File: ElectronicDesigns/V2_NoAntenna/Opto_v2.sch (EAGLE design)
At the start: 7 parts, among them U1 TLV1117-18IDCYG3

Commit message: Presentation
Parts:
- removed C2: 06036D225KAT2A, Capacitor_2.2uF_0603:06036D225KAT2A
- removed U$2: B220A-13-F, Schottky_0603:B220A-13-F
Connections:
- removed net IN-: C1.2, U$2.C
- net GND: now also C1.2; no longer C2.2, U$2.A
- net N$4: no longer C2.1
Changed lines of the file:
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@@
 <parts>
 <part name="GND1" library="supply1" library_urn="urn:adsk.eagle:library:371" deviceset="GND" device=""/>
-<part name="GND2" library="supply1" library_urn="urn:adsk.eagle:library:371" deviceset="GND" device=""/>
 <part name="R1" library="CRCW06033K30FKEA" deviceset="CRCW06033K30FKEA" device=""/>
 <part name="U1" library="TLV1117-18IDCYG3" deviceset="TLV1117-18IDCYG3" device=""/>
 <part name="U$1" library="Schottky_0603" deviceset="B220A-13-F" device=""/>
-<part name="U$2" library="Schottky_0603" deviceset="B220A-13-F" device=""/>
 <part name="C1" library="Capacitor_2.2uF_0603" deviceset="06036D225KAT2A" device=""/>
-<part name="C2" library="Capacitor_2.2uF_0603" deviceset="06036D225KAT2A" device=""/>
 <part name="U$3" library="LEDM1608X80" deviceset="LED" device=""/>
 </parts>
@@
 </plain>
 <instances>
-<instance part="GND1" gate="1" x="40.64" y="35.56"/>
-<instance part="GND2" gate="1" x="88.9" y="35.56"/>
+<instance part="GND1" gate="1" x="48.26" y="35.56"/>
 <instance part="R1" gate="G$1" x="114.3" y="63.5"/>
 <instance part="U1" gate="A" x="68.58" y="66.04"/>
 <instance part="U$1" gate="A" x="10.16" y="71.12"/>
-<instance part="U$2" gate="A" x="12.7" y="43.18" rot="R180"/>
 <instance part="C1" gate="G$1" x="-10.16" y="55.88" rot="R90"/>
-<instance part="C2" gate="G$1" x="30.48" y="55.88" rot="R90"/>
 <instance part="U$3" gate="G$1" x="137.16" y="63.5"/>
 </instances>
@@
 </segment>
 </net>
-<net name="IN-" class="0">
-<segment>
-<wire x1="10.16" y1="43.18" x2="-10.16" y2="43.18" width="0.1524" layer="91"/>
-<label x="-35.56" y="43.18" size="1.778" layer="95" rot="R180" xref="yes"/>
-<pinref part="U$2" gate="A" pin="C"/>
-<pinref part="C1" gate="G$1" pin="2"/>
-<wire x1="-10.16" y1="43.18" x2="-35.56" y2="43.18" width="0.1524" layer="91"/>
-<wire x1="-10.16" y1="53.34" x2="-10.16" y2="43.18" width="0.1524" layer="91"/>
-<junction x="-10.16" y="43.18"/>
-</segment>
-</net>
 <net name="N$4" class="0">
 <segment>
-<wire x1="48.26" y1="71.12" x2="30.48" y2="71.12" width="0.1524" layer="91"/>
 <pinref part="U1" gate="A" pin="INPUT"/>
-<wire x1="30.48" y1="71.12" x2="12.7" y2="71.12" width="0.1524" layer="91"/>
+<wire x1="48.26" y1="71.12" x2="12.7" y2="71.12" width="0.1524" layer="91"/>
 <wire x1="48.26" y1="66.04" x2="48.26" y2="71.12" width="0.1524" layer="91"/>
 <pinref part="U$1" gate="A" pin="C"/>
-<pinref part="C2" gate="G$1" pin="1"/>
-<wire x1="30.48" y1="60.96" x2="30.48" y2="71.12" width="0.1524" layer="91"/>
-<junction x="30.48" y="71.12"/>
-</segment>
-</net>
-<net name="GND" class="0">
-<segment>
-<wire x1="15.24" y1="43.18" x2="30.48" y2="43.18" width="0.1524" layer="91"/>
-<junction x="40.64" y="43.18"/>
-<pinref part="GND1" gate="1" pin="GND"/>
-<wire x1="30.48" y1="43.18" x2="40.64" y2="43.18" width="0.1524" layer="91"/>
-<wire x1="40.64" y1="38.1" x2="40.64" y2="43.18" width="0.1524" layer="91"/>
-<pinref part="U1" gate="A" pin="ADJ/GND"/>
-<wire x1="48.26" y1="58.42" x2="48.26" y2="43.18" width="0.1524" layer="91"/>
-<wire x1="48.26" y1="43.18" x2="40.64" y2="43.18" width="0.1524" layer="91"/>
-<pinref part="U$2" gate="A" pin="A"/>
-<pinref part="C2" gate="G$1" pin="2"/>
-<wire x1="30.48" y1="53.34" x2="30.48" y2="43.18" width="0.1524" layer="91"/>
-<junction x="30.48" y="43.18"/>
-</segment>
-<segment>
-<pinref part="GND2" gate="1" pin="GND"/>
-<wire x1="88.9" y1="38.1" x2="88.9" y2="53.34" width="0.1524" layer="91"/>
-<wire x1="154.94" y1="63.5" x2="154.94" y2="53.34" width="0.1524" layer="91"/>
-<wire x1="154.94" y1="53.34" x2="88.9" y2="53.34" width="0.1524" layer="91"/>
-<pinref part="U$3" gate="G$1" pin="OUT"/>
-<wire x1="147.32" y1="63.5" x2="154.94" y2="63.5" width="0.1524" layer="91"/>
 </segment>
 </net>
@@
 </segment>
 </net>
+<net name="GND" class="0">
+<segment>
+<pinref part="U1" gate="A" pin="ADJ/GND"/>
+<wire x1="48.26" y1="58.42" x2="48.26" y2="43.18" width="0.1524" layer="91"/>
+<wire x1="48.26" y1="43.18" x2="-10.16" y2="43.18" width="0.1524" layer="91"/>
+<label x="-35.56" y="43.18" size="1.778" layer="95" rot="R180" xref="yes"/>
+<pinref part="C1" gate="G$1" pin="2"/>
+<wire x1="-10.16" y1="43.18" x2="-35.56" y2="43.18" width="0.1524" layer="91"/>
+<wire x1="-10.16" y1="53.34" x2="-10.16" y2="43.18" width="0.1524" layer="91"/>
+<junction x="-10.16" y="43.18"/>
+<pinref part="U$3" gate="G$1" pin="OUT"/>
+<wire x1="147.32" y1="63.5" x2="154.94" y2="63.5" width="0.1524" layer="91"/>
+<wire x1="154.94" y1="63.5" x2="154.94" y2="43.18" width="0.1524" layer="91"/>
+<wire x1="154.94" y1="43.18" x2="48.26" y2="43.18" width="0.1524" layer="91"/>
+<junction x="48.26" y="43.18"/>
+<pinref part="GND1" gate="1" pin="GND"/>
+<wire x1="48.26" y1="38.1" x2="48.26" y2="43.18" width="0.1524" layer="91"/>
+</segment>
+</net>

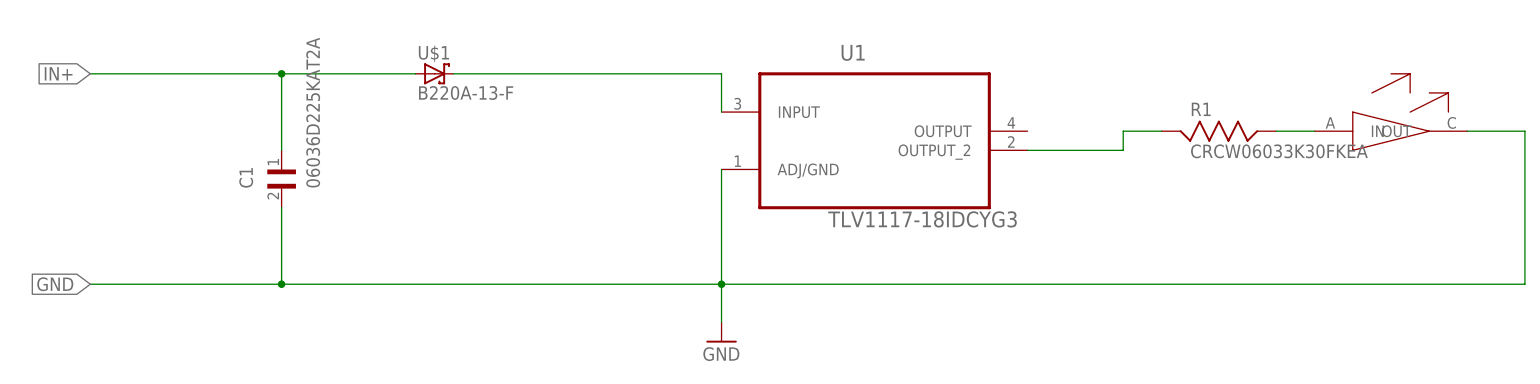
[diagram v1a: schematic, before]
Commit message: antenna-circuit assembled
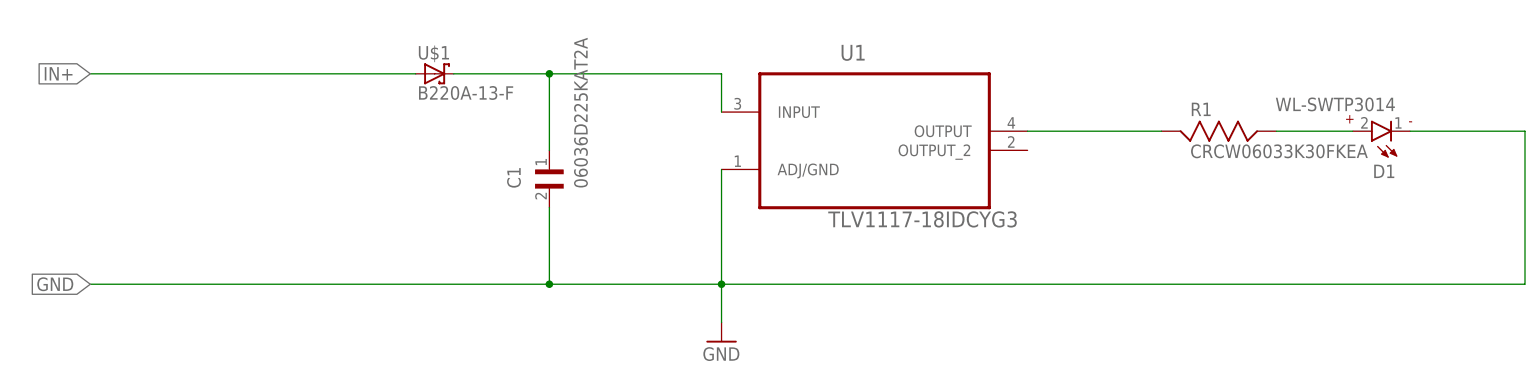
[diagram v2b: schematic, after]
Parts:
- removed U$3: LED, LEDM1608X80:LED
- added D1: WL-SWTP3014, WL-SWTP:WL-SWTP3014
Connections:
- net GND: now also D1.1; no longer U$3.OUT
- net IN+: no longer C1.1
- net N$1: now also U1.OUTPUT; no longer U1.OUTPUT_2
- net N$2: now also D1.2; no longer U$3.IN
- net N$4: now also C1.1
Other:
- moved on the sheet: C1
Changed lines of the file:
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@@
 <part name="U$1" library="Schottky_0603" deviceset="B220A-13-F" device=""/>
 <part name="C1" library="Capacitor_2.2uF_0603" deviceset="06036D225KAT2A" device=""/>
-<part name="U$3" library="LEDM1608X80" deviceset="LED" device=""/>
+<part name="D1" library="WL-SWTP" deviceset="WL-SWTP" device="3014"/>
 </parts>
 <sheets>
@@
 <instance part="U1" gate="A" x="68.58" y="66.04"/>
 <instance part="U$1" gate="A" x="10.16" y="71.12"/>
-<instance part="C1" gate="G$1" x="-10.16" y="55.88" rot="R90"/>
-<instance part="U$3" gate="G$1" x="137.16" y="63.5"/>
+<instance part="C1" gate="G$1" x="25.4" y="55.88" rot="R90"/>
+<instance part="D1" gate="G$1" x="137.16" y="63.5" rot="R180"/>
 </instances>
 <busses>
@@
 <net name="IN+" class="0">
 <segment>
-<wire x1="7.62" y1="71.12" x2="-10.16" y2="71.12" width="0.1524" layer="91"/>
 <label x="-35.56" y="71.12" size="1.778" layer="95" rot="R180" xref="yes"/>
 <pinref part="U$1" gate="A" pin="A"/>
-<pinref part="C1" gate="G$1" pin="1"/>
-<wire x1="-10.16" y1="71.12" x2="-35.56" y2="71.12" width="0.1524" layer="91"/>
-<wire x1="-10.16" y1="60.96" x2="-10.16" y2="71.12" width="0.1524" layer="91"/>
-<junction x="-10.16" y="71.12"/>
+<wire x1="7.62" y1="71.12" x2="-35.56" y2="71.12" width="0.1524" layer="91"/>
 </segment>
 </net>
@@
 <segment>
 <pinref part="U1" gate="A" pin="INPUT"/>
-<wire x1="48.26" y1="71.12" x2="12.7" y2="71.12" width="0.1524" layer="91"/>
+<wire x1="48.26" y1="71.12" x2="25.4" y2="71.12" width="0.1524" layer="91"/>
+<wire x1="25.4" y1="71.12" x2="12.7" y2="71.12" width="0.1524" layer="91"/>
 <wire x1="48.26" y1="66.04" x2="48.26" y2="71.12" width="0.1524" layer="91"/>
 <pinref part="U$1" gate="A" pin="C"/>
+<pinref part="C1" gate="G$1" pin="1"/>
+<wire x1="25.4" y1="60.96" x2="25.4" y2="71.12" width="0.1524" layer="91"/>
+<junction x="25.4" y="71.12"/>
 </segment>
 </net>
 <net name="N$1" class="0">
 <segment>
-<pinref part="U1" gate="A" pin="OUTPUT_2"/>
-<wire x1="88.9" y1="60.96" x2="101.6" y2="60.96" width="0.1524" layer="91"/>
-<wire x1="101.6" y1="60.96" x2="101.6" y2="63.5" width="0.1524" layer="91"/>
 <pinref part="R1" gate="G$1" pin="1"/>
-<wire x1="101.6" y1="63.5" x2="106.68" y2="63.5" width="0.1524" layer="91"/>
-</segment>
-</net>
-<net name="N$2" class="0">
-<segment>
-<pinref part="U$3" gate="G$1" pin="IN"/>
-<pinref part="R1" gate="G$1" pin="2"/>
-<wire x1="127" y1="63.5" x2="121.92" y2="63.5" width="0.1524" layer="91"/>
+<pinref part="U1" gate="A" pin="OUTPUT"/>
+<wire x1="88.9" y1="63.5" x2="106.68" y2="63.5" width="0.1524" layer="91"/>
 </segment>
 </net>
@@
 <pinref part="U1" gate="A" pin="ADJ/GND"/>
 <wire x1="48.26" y1="58.42" x2="48.26" y2="43.18" width="0.1524" layer="91"/>
-<wire x1="48.26" y1="43.18" x2="-10.16" y2="43.18" width="0.1524" layer="91"/>
+<wire x1="48.26" y1="43.18" x2="25.4" y2="43.18" width="0.1524" layer="91"/>
 <label x="-35.56" y="43.18" size="1.778" layer="95" rot="R180" xref="yes"/>
-<pinref part="C1" gate="G$1" pin="2"/>
-<wire x1="-10.16" y1="43.18" x2="-35.56" y2="43.18" width="0.1524" layer="91"/>
-<wire x1="-10.16" y1="53.34" x2="-10.16" y2="43.18" width="0.1524" layer="91"/>
-<junction x="-10.16" y="43.18"/>
-<pinref part="U$3" gate="G$1" pin="OUT"/>
-<wire x1="147.32" y1="63.5" x2="154.94" y2="63.5" width="0.1524" layer="91"/>
+<wire x1="25.4" y1="43.18" x2="-35.56" y2="43.18" width="0.1524" layer="91"/>
 <wire x1="154.94" y1="63.5" x2="154.94" y2="43.18" width="0.1524" layer="91"/>
 <wire x1="154.94" y1="43.18" x2="48.26" y2="43.18" width="0.1524" layer="91"/>
@@
 <pinref part="GND1" gate="1" pin="GND"/>
 <wire x1="48.26" y1="38.1" x2="48.26" y2="43.18" width="0.1524" layer="91"/>
+<pinref part="C1" gate="G$1" pin="2"/>
+<wire x1="25.4" y1="53.34" x2="25.4" y2="43.18" width="0.1524" layer="91"/>
+<junction x="25.4" y="43.18"/>
+<pinref part="D1" gate="G$1" pin="1"/>
+<wire x1="139.7" y1="63.5" x2="154.94" y2="63.5" width="0.1524" layer="91"/>
 </segment>
 </net>
+<net name="N$2" class="0">
+<segment>
+<pinref part="R1" gate="G$1" pin="2"/>
+<pinref part="D1" gate="G$1" pin="2"/>
+<wire x1="121.92" y1="63.5" x2="132.08" y2="63.5" width="0.1524" layer="91"/>
+</segment>
+</net>
